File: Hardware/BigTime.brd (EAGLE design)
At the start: 43.2 x 43.2 mm, 14 parts, among them U1 ATMEGA328P_PDIP_EZ, Y1 32.768kHz

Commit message: Mods for threaded inserts, PTH battery holder. - Modified .sch and .brd files to V13 to add PTH battery holder. - Modified enclosure file to change thickness of layer 1 and hole    sizes on layer 1 to 3.9mm.
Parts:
- BAT: device Testing:BATTCON_20MM_4LEGS -> SparkFun-Electromechanical:BATTERY_20MM_PTH_COMPACT
- turned BAT to 180 degrees
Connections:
- net VCC: no longer BAT.3, BAT.P$1, BAT.P$2
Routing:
- net VCC: track 101.5 -> 77.9 mm
- net GND: track 91.6 -> 94.6 mm
- removed copper zone on layer 1, net VCC
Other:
- board text added: "v14"
- board text removed: "v13"

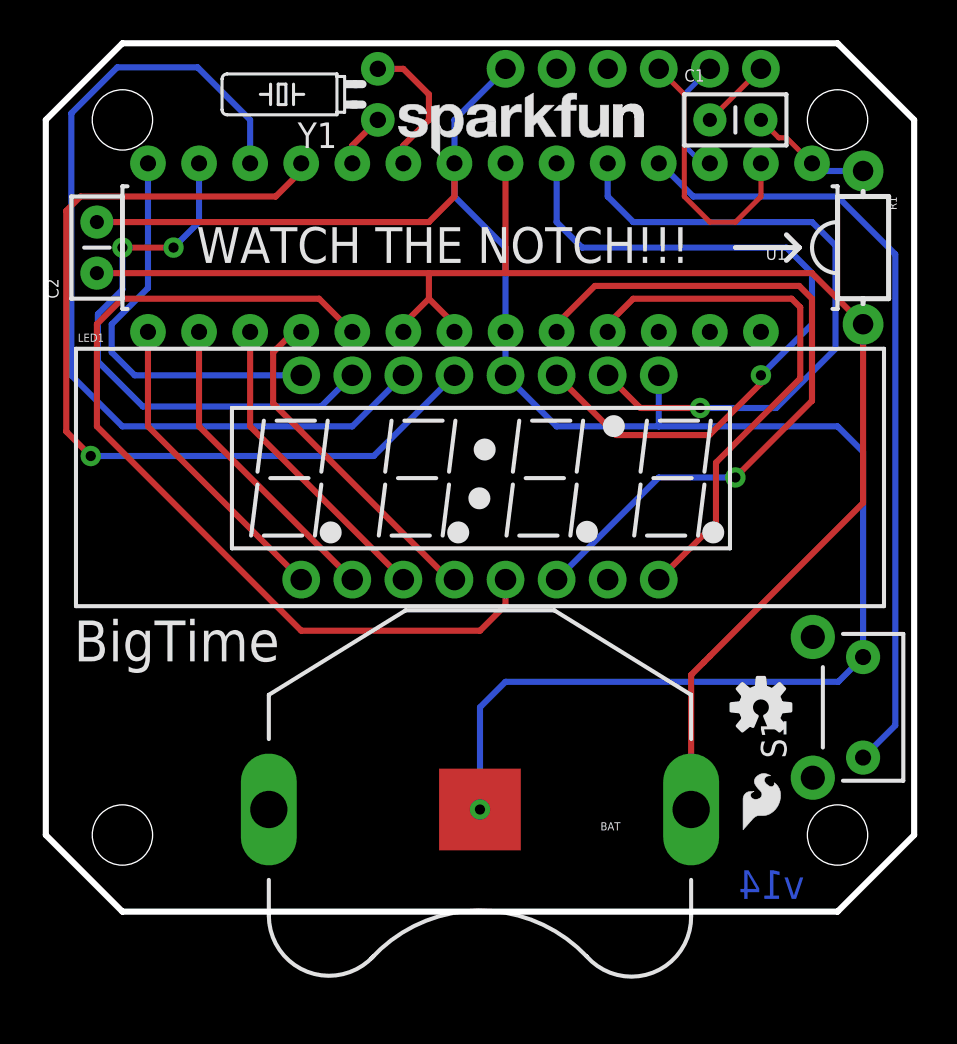
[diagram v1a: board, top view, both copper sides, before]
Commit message: Tweaks to board, enclosure, repo - Enclosure:  * Hole size in layer 1 is now right for threaded inserts  * Change thickness note on layers 2 and 3 to 1/8"  * Moved lever from center of layer 3 to ensure thickness of plastic would be the same - Board:  * Tweak battery holder down slightly, as it was interfering with display  * Change to rev 15 - Repo: move enclosure file to top level, per SparkFun standards
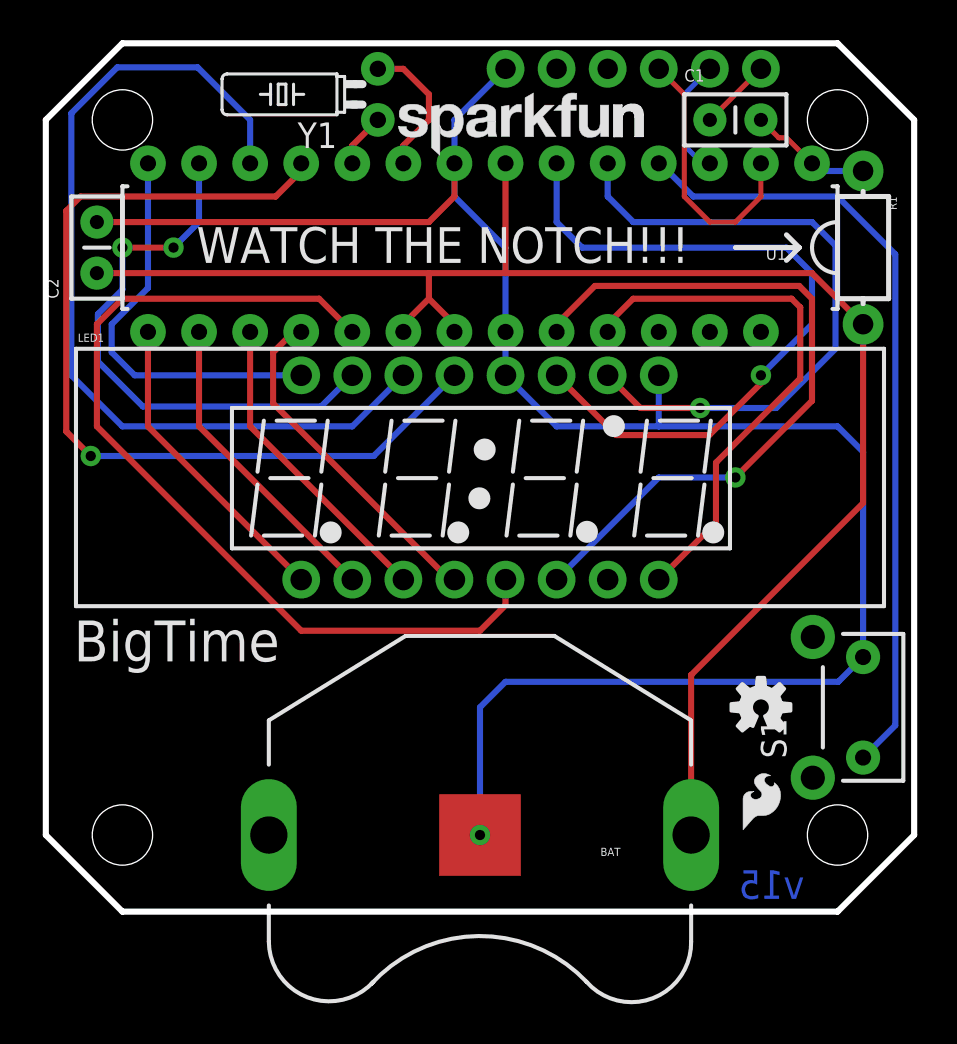
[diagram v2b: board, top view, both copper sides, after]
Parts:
- moved BAT 1.27 mm to (21.6, 3.81)
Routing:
- net GND: track 94.6 -> 95.8 mm
- net VCC: track 77.9 -> 79.2 mm
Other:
- board text added: "v15"
- board text removed: "v14"
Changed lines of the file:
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@@
 <?xml version="1.0" encoding="utf-8"?>
 <!DOCTYPE eagle SYSTEM "eagle.dtd">
-<eagle version="6.3">
+<eagle version="6.4">
 <drawing>
 <settings>
@@
 <wire x1="39.37" y1="0" x2="43.18" y2="3.81" width="0.3048" layer="20"/>
 <text x="1.397" y="12.446" size="2.032" layer="21" font="vector" ratio="15">BigTime</text>
-<text x="37.719" y="0.635" size="1.4224" layer="16" font="vector" ratio="15" rot="MR0">v14</text>
+<text x="37.719" y="0.635" size="1.4224" layer="16" font="vector" ratio="15" rot="MR0">v15</text>
 <text x="25.4" y="-10.16" size="1.778" layer="48" font="vector" ratio="15">N. Seidle</text>
 <text x="36.83" y="42.418" size="1.016" layer="22" font="vector" ratio="15" rot="MR180">GRN</text>
@@
 <element name="Y1" library="SparkFun-FreqCtrl" package="TC26HEZ" value="32.768kHz" x="16.51" y="40.64" rot="R90"/>
 <element name="S1" library="SparkFun-Electromechanical" package="TACTILE-PTH-SIDEEZ" value="BUTTON" x="40.64" y="10.16" rot="R90"/>
-<element name="BAT" library="SparkFun-Electromechanical" package="BATTERY_20MM_PTH_COMPACT" value="" x="21.59" y="5.08" rot="R180"/>
+<element name="BAT" library="SparkFun-Electromechanical" package="BATTERY_20MM_PTH_COMPACT" value="" x="21.59" y="3.81" rot="R180"/>
 </elements>
 <signals>
@@
 <wire x1="40.64" y1="12.66" x2="40.64" y2="22.86" width="0.3048" layer="16"/>
 <contactref element="BAT" pad="2"/>
-<via x="21.59" y="5.08" extent="1-16" drill="0.508"/>
-<wire x1="21.59" y1="5.08" x2="21.59" y2="10.16" width="0.3048" layer="16"/>
+<via x="21.59" y="3.81" extent="1-16" drill="0.508"/>
+<wire x1="21.59" y1="3.81" x2="21.59" y2="10.16" width="0.3048" layer="16"/>
 <wire x1="21.59" y1="10.16" x2="22.86" y2="11.43" width="0.3048" layer="16"/>
 <wire x1="22.86" y1="11.43" x2="39.41" y2="11.43" width="0.3048" layer="16"/>
@@
 <wire x1="19.05" y1="31.75" x2="22.86" y2="31.75" width="0.3048" layer="1"/>
 <wire x1="22.86" y1="31.75" x2="38.1" y2="31.75" width="0.3048" layer="1"/>
-<wire x1="40.64" y1="20.32" x2="33.02" y2="12.7" width="0.3048" layer="1"/>
+<wire x1="40.64" y1="20.32" x2="32.09" y2="11.77" width="0.3048" layer="1"/>
 <contactref element="U1" pad="21"/>
 <contactref element="U1" pad="7"/>
 <contactref element="U1" pad="20"/>
-<wire x1="33.02" y1="12.7" x2="32.717" y2="12.397" width="0.3048" layer="1"/>
 <wire x1="17.78" y1="28.829" x2="17.78" y2="29.21" width="0.3048" layer="1"/>
 <wire x1="17.78" y1="29.21" x2="19.05" y2="30.48" width="0.3048" layer="1"/>
@@
 <wire x1="2.54" y1="31.75" x2="19.05" y2="31.75" width="0.3048" layer="1"/>
 <contactref element="BAT" pad="1"/>
-<wire x1="32.09" y1="5.08" x2="32.09" y2="11.77" width="0.3048" layer="1"/>
-<wire x1="32.09" y1="11.77" x2="32.717" y2="12.397" width="0.3048" layer="1"/>
+<wire x1="32.09" y1="3.81" x2="32.09" y2="11.77" width="0.3048" layer="1"/>
 </signal>
 <signal name="AMPM">
